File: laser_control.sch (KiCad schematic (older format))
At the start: 20 parts, among them J1 DB9, P1 CONN_01X05, Q1 BC846A, Q2 BC846A, U1 74HCT02, U2 H11L1, U3 H11L1

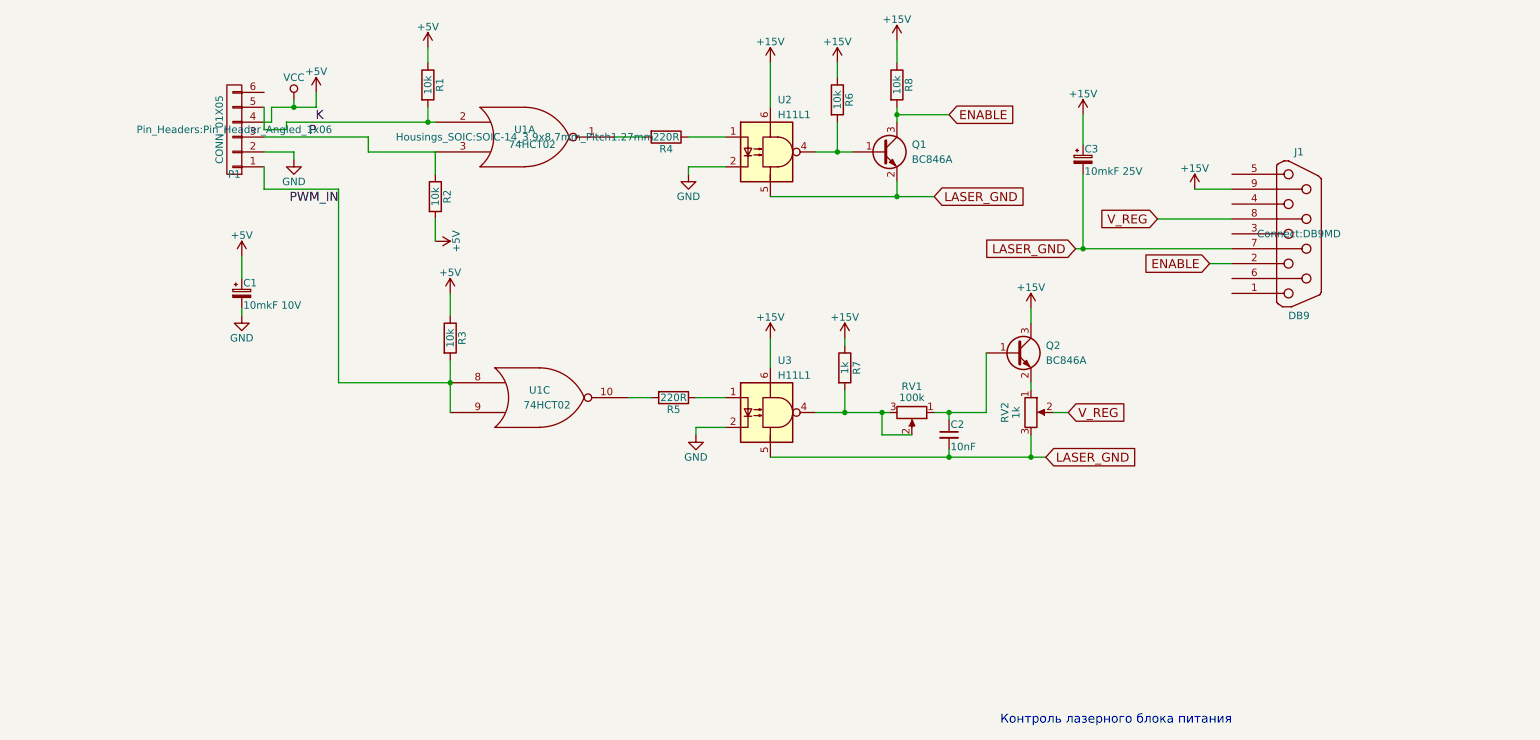
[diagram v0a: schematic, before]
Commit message: Minimal viable modifications
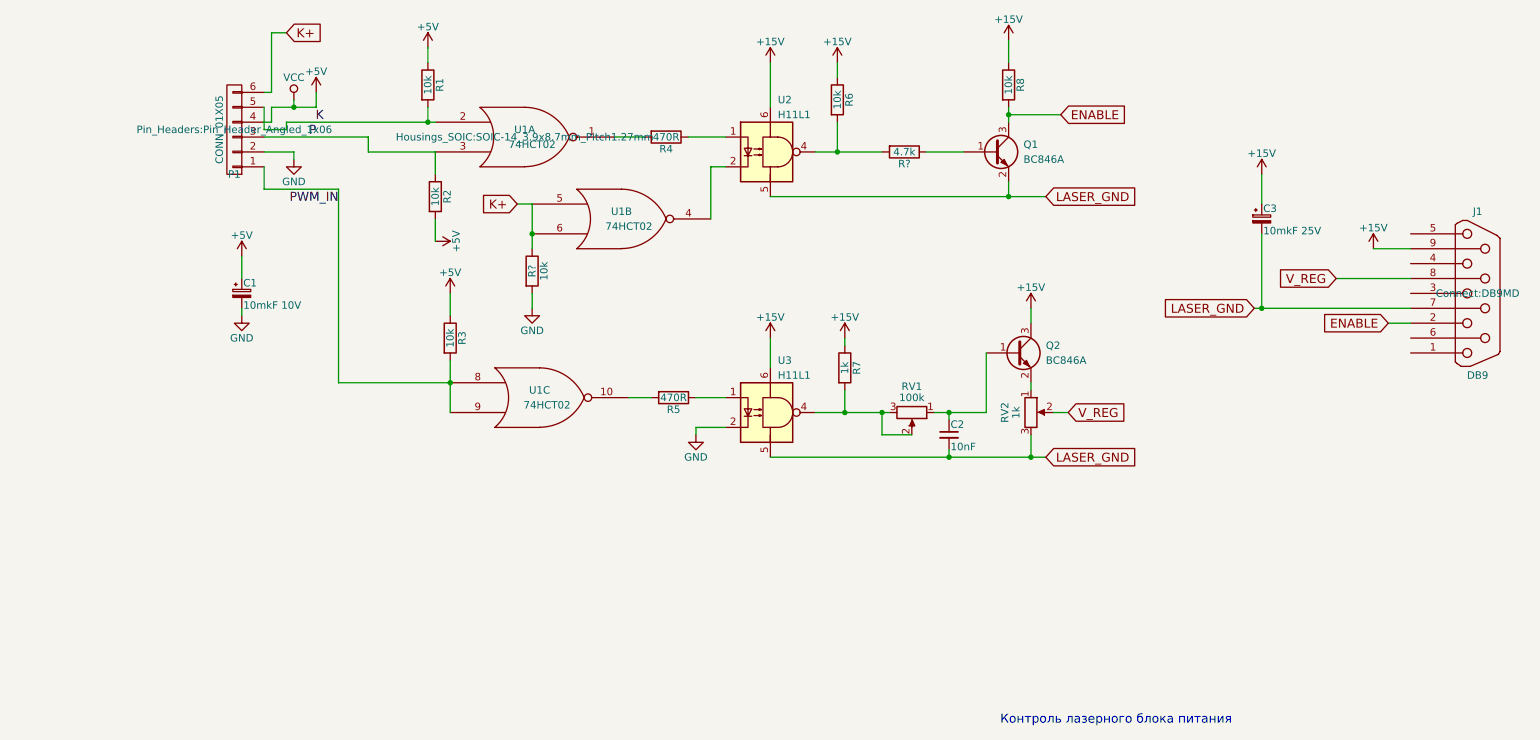
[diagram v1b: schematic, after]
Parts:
- added 10k: R?, Resistors_SMD:R_0805_HandSoldering, symbol R
- added R?: 4.7k, Resistors_SMD:R_0805_HandSoldering, symbol R
- added unit 2 of U1
- R4, R5: value 220R -> 470R
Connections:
- net +5V: now also U1.14 (VCC)
- net GND: now also 10k.2, U1.7 (GND); no longer U2.2
- net at R6.2, U2.4: now also R?.2; no longer Q1.1 (B)
- net K+: now reaches P1.6 (P6)
- net K+: now also 10k.1, U1.5, U1.6
- new net: U1.4, U2.2
- new net: Q1.1 (B), R?.1
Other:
- moved on the sheet: C3, J1, Q1, R8
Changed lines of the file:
@@
 L DB9 J1
 U 1 1 5C063D4D
-P 9500 4200
-F 0 "J1" H 9500 4750 50  0000 C CNN
-F 1 "DB9" H 9500 3650 50  0000 C CNN
-F 2 "Connect:DB9MD" H 9500 4200 50  0000 C CNN
-F 3 "" H 9500 4200 50  0000 C CNN
-	1    9500 4200
+P 10700 4600
+F 0 "J1" H 10700 5150 50  0000 C CNN
+F 1 "DB9" H 10700 4050 50  0000 C CNN
+F 2 "Connect:DB9MD" H 10700 4600 50  0000 C CNN
+F 3 "" H 10700 4600 50  0000 C CNN
+	1    10700 4600
 	1    0    0    -1
 $EndComp
@@
 L Q_NPN_BEC Q1
 U 1 1 5C063F42
-P 6700 3650
-F 0 "Q1" H 6900 3700 50  0000 L CNN
-F 1 "BC846A" H 6900 3600 50  0000 L CNN
-F 2 "TO_SOT_Packages_SMD:SOT-23" H 6900 3750 50  0001 C CNN
-F 3 "" H 6700 3650 50  0001 C CNN
-	1    6700 3650
+P 7450 3650
+F 0 "Q1" H 7650 3700 50  0000 L CNN
+F 1 "BC846A" H 7650 3600 50  0000 L CNN
+F 2 "TO_SOT_Packages_SMD:SOT-23" H 7650 3750 50  0001 C CNN
+F 3 "" H 7450 3650 50  0001 C CNN
+	1    7450 3650
 	1    0    0    -1
 $EndComp
@@
 L +15V #PWR01
 U 1 1 5C064296
-P 8800 3900
-F 0 "#PWR01" H 8800 3750 50  0001 C CNN
-F 1 "+15V" H 8800 4040 50  0000 C CNN
-F 2 "" H 8800 3900 50  0001 C CNN
-F 3 "" H 8800 3900 50  0001 C CNN
-	1    8800 3900
+P 10000 4300
+F 0 "#PWR01" H 10000 4150 50  0001 C CNN
+F 1 "+15V" H 10000 4440 50  0000 C CNN
+F 2 "" H 10000 4300 50  0001 C CNN
+F 3 "" H 10000 4300 50  0001 C CNN
+	1    10000 4300
 	1    0    0    -1
 $EndComp
@@
 L R R8
 U 1 1 5C064446
-P 6800 3200
-F 0 "R8" V 6880 3200 50  0000 C CNN
-F 1 "10k" V 6800 3200 50  0000 C CNN
-F 2 "Resistors_ThroughHole:Resistor_Horizontal_RM10mm" V 6730 3200 50  0001 C CNN
-F 3 "" H 6800 3200 50  0001 C CNN
-	1    6800 3200
+P 7550 3200
+F 0 "R8" V 7630 3200 50  0000 C CNN
+F 1 "10k" V 7550 3200 50  0000 C CNN
+F 2 "Resistors_ThroughHole:Resistor_Horizontal_RM10mm" V 7480 3200 50  0001 C CNN
+F 3 "" H 7550 3200 50  0001 C CNN
+	1    7550 3200
 	1    0    0    -1
 $EndComp
@@
 L +15V #PWR05
 U 1 1 5C06450F
-P 6800 2900
-F 0 "#PWR05" H 6800 2750 50  0001 C CNN
-F 1 "+15V" H 6800 3040 50  0000 C CNN
-F 2 "" H 6800 2900 50  0001 C CNN
-F 3 "" H 6800 2900 50  0001 C CNN
-	1    6800 2900
-	1    0    0    -1
-$EndComp
-Text GLabel 7050 3950 2    60   Input ~ 0
+P 7550 2900
+F 0 "#PWR05" H 7550 2750 50  0001 C CNN
+F 1 "+15V" H 7550 3040 50  0000 C CNN
+F 2 "" H 7550 2900 50  0001 C CNN
+F 3 "" H 7550 2900 50  0001 C CNN
+	1    7550 2900
+	1    0    0    -1
+$EndComp
+Text GLabel 7800 3950 2    60   Input ~ 0
 LASER_GND
-Text GLabel 8000 4300 0    60   Input ~ 0
+Text GLabel 9200 4700 0    60   Input ~ 0
 LASER_GND
-Text GLabel 7150 3400 2    60   Input ~ 0
+Text GLabel 7900 3400 2    60   Input ~ 0
 ENABLE
-Text GLabel 8900 4400 0    60   Input ~ 0
+Text GLabel 10100 4800 0    60   Input ~ 0
 ENABLE
-Text GLabel 8550 4100 0    60   Input ~ 0
+Text GLabel 9750 4500 0    60   Input ~ 0
 V_REG
 $Comp
@@
 P 5250 3550
 F 0 "R4" V 5330 3550 50  0000 C CNN
-F 1 "220R" V 5250 3550 50  0000 C CNN
+F 1 "470R" V 5250 3550 50  0000 C CNN
 F 2 "Resistors_SMD:R_0805_HandSoldering" V 5180 3550 50  0001 C CNN
 F 3 "" H 5250 3550 50  0001 C CNN
@@
 LASER_GND
 Wire Wire Line
-	6250 3650 6500 3650
+	6250 3650 6700 3650
 Connection ~ 6400 3650
 Wire Wire Line
-	8000 4300 9050 4300
-Wire Wire Line
-	6800 3850 6800 3950
-Wire Wire Line
-	8800 3900 9050 3900
+	9200 4700 10250 4700
+Wire Wire Line
+	7550 3850 7550 3950
+Wire Wire Line
+	10000 4300 10250 4300
 Wire Wire Line
 	6400 3050 6400 3150
@@
 	5950 4900 5950 5100
 Wire Wire Line
-	6800 3350 6800 3450
-Wire Wire Line
-	6800 2900 6800 3050
-Wire Wire Line
-	5950 3950 7050 3950
-Connection ~ 6800 3950
-Wire Wire Line
-	6400 3450 6400 3650
-Wire Wire Line
-	6800 3400 7150 3400
-Connection ~ 6800 3400
-Wire Wire Line
-	8900 4400 9050 4400
-Wire Wire Line
-	8550 4100 9050 4100
+	7550 3350 7550 3450
+Wire Wire Line
+	7550 2900 7550 3050
+Wire Wire Line
+	5950 3950 7800 3950
+Connection ~ 7550 3950
+Wire Wire Line
+	6400 3650 6400 3450
+Wire Wire Line
+	7550 3400 7900 3400
+Connection ~ 7550 3400
+Wire Wire Line
+	10100 4800 10250 4800
+Wire Wire Line
+	9750 4500 10250 4500
 Wire Wire Line
 	5400 3550 5650 3550
@@
 P 5300 5300
 F 0 "R5" V 5380 5300 50  0000 C CNN
-F 1 "220R" V 5300 5300 50  0000 C CNN
+F 1 "470R" V 5300 5300 50  0000 C CNN
 F 2 "Resistors_SMD:R_0805_HandSoldering" V 5230 5300 50  0001 C CNN
 F 3 "" H 5300 5300 50  0001 C CNN
@@
 	3800 5050 3800 5400
 Wire Wire Line
-	5400 3750 5650 3750
-Wire Wire Line
-	5400 3750 5400 3800
-Wire Wire Line
 	5650 5500 5450 5500
 Wire Wire Line
 	5450 5500 5450 5550
-$Comp
-L GND #PWR07
-U 1 1 5C0659F6
-P 5400 3800
-F 0 "#PWR07" H 5400 3550 50  0001 C CNN
-F 1 "GND" H 5400 3650 50  0000 C CNN
-F 2 "" H 5400 3800 50  0001 C CNN
-F 3 "" H 5400 3800 50  0001 C CNN
-	1    5400 3800
-	1    0    0    -1
-$EndComp
 $Comp
 L GND #PWR08
@@
 L CP_Small C3
 U 1 1 5C0675C7
-P 8050 3700
-F 0 "C3" H 8060 3770 50  0000 L CNN
-F 1 "10mkF 25V" H 8060 3620 50  0000 L CNN
-F 2 "Capacitors_SMD:c_elec_6.3x5.3" H 8050 3700 50  0001 C CNN
-F 3 "" H 8050 3700 50  0001 C CNN
-	1    8050 3700
+P 9250 4100
+F 0 "C3" H 9260 4170 50  0000 L CNN
+F 1 "10mkF 25V" H 9260 4020 50  0000 L CNN
+F 2 "Capacitors_SMD:c_elec_6.3x5.3" H 9250 4100 50  0001 C CNN
+F 3 "" H 9250 4100 50  0001 C CNN
+	1    9250 4100
 	1    0    0    -1
 $EndComp
@@
 L +15V #PWR017
 U 1 1 5C067662
-P 8050 3400
-F 0 "#PWR017" H 8050 3250 50  0001 C CNN
-F 1 "+15V" H 8050 3540 50  0000 C CNN
-F 2 "" H 8050 3400 50  0001 C CNN
-F 3 "" H 8050 3400 50  0001 C CNN
-	1    8050 3400
-	1    0    0    -1
-$EndComp
-Wire Wire Line
-	8050 3800 8050 4300
-Connection ~ 8050 4300
-Wire Wire Line
-	8050 3400 8050 3600
+P 9250 3800
+F 0 "#PWR017" H 9250 3650 50  0001 C CNN
+F 1 "+15V" H 9250 3940 50  0000 C CNN
+F 2 "" H 9250 3800 50  0001 C CNN
+F 3 "" H 9250 3800 50  0001 C CNN
+	1    9250 3800
+	1    0    0    -1
+$EndComp
+Wire Wire Line
+	9250 4200 9250 4700
+Connection ~ 9250 4700
+Wire Wire Line
+	9250 3800 9250 4000
 Text Notes 9050 7500 2    60   ~ 0
 Контроль лазерного блока питания
@@
 Wire Wire Line
 	2750 3650 2550 3650
+$Comp
+L 74HCT02 U1
+U 2 1 5C276FC0
+P 4950 4100
+F 0 "U1" H 4950 4150 50  0000 C CNN
+F 1 "74HCT02" H 5000 4050 50  0000 C CNN
+F 2 "" H 4950 4100 50  0000 C CNN
+F 3 "" H 4950 4100 50  0000 C CNN
+	2    4950 4100
+	1    0    0    -1
+$EndComp
+Wire Wire Line
+	4350 4000 4350 4300
+$Comp
+L R 10k
+U 1 1 5C277267
+P 4350 4450
+F 0 "10k" V 4430 4450 50  0000 C CNN
+F 1 "R?" V 4350 4450 50  0000 C CNN
+F 2 "Resistors_SMD:R_0805_HandSoldering" V 4280 4450 50  0001 C CNN
+F 3 "" H 4350 4450 50  0001 C CNN
+	1    4350 4450
+	1    0    0    -1
+$EndComp
+Connection ~ 4350 4200
+Wire Wire Line
+	4350 4600 4350 4700
+$Comp
+L GND #PWR?
+U 1 1 5C2773F5
+P 4350 4700
+F 0 "#PWR?" H 4350 4450 50  0001 C CNN
+F 1 "GND" H 4350 4550 50  0000 C CNN
+F 2 "" H 4350 4700 50  0001 C CNN
+F 3 "" H 4350 4700 50  0001 C CNN
+	1    4350 4700
+	1    0    0    -1
+$EndComp
+Wire Wire Line
+	2550 3250 2600 3250
+Wire Wire Line
+	2600 3250 2600 2850
+Wire Wire Line
+	2600 2850 2700 2850
+Text GLabel 2700 2850 2    60   Input ~ 0
+K+
+Wire Wire Line
+	5650 3750 5550 3750
+Wire Wire Line
+	5550 3750 5550 4100
+Wire Wire Line
+	4350 4000 4250 4000
+Text GLabel 4250 4000 0    60   Input ~ 0
+K+
+$Comp
+L R R?
+U 1 1 5C277CF8
+P 6850 3650
+F 0 "R?" V 6930 3650 50  0000 C CNN
+F 1 "4.7k" V 6850 3650 50  0000 C CNN
+F 2 "Resistors_SMD:R_0805_HandSoldering" V 6780 3650 50  0001 C CNN
+F 3 "" H 6850 3650 50  0001 C CNN
+	1    6850 3650
+	0    1    1    0
+$EndComp
+Wire Wire Line
+	7000 3650 7250 3650
 $EndSCHEMATC

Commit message: Control with feedback
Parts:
- removed Q2: BC846A, TO_SOT_Packages_SMD:SOT-23, symbol Q_NPN_BEC
- added C4: 0.47uF, Capacitors_SMD:C_0805_HandSoldering, symbol C
- added R10: 100k, Resistors_ThroughHole:Resistor_Horizontal_RM10mm, symbol R
- added S1: button1, local:button1, symbol button1
- added U4: LM358, Housings_SOIC:SOIC-8_3.9x4.9mm_Pitch1.27mm, symbol LM358
- R11: renamed from 10k; value R? -> 10k; footprint Resistors_SMD:R_0805_HandSoldering -> Resistors_ThroughHole:Resistor_Horizontal_RM10mm
- R7: footprint Resistors_ThroughHole:Resistor_Horizontal_RM10mm -> Resistors_SMD:R_0805_HandSoldering
- gave numbers to parts that had none: 1
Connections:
- net +15V: now also U4.8 (V+), U4.8 (V+)
- net +5V: now also S1.5; no longer R3.1
- net GND: now also R3.1, S1.2
- net K: now also U1.5, S1.3; no longer U1.2
- net K+: now also U1.2, U1.3, S1.4; no longer U1.5, U1.6
- net LASER_GND: now also U4.4 (V-), U4.4 (V-)
- net P: now also U1.6; no longer U1.3
- net V_REG: now also C4.1, U4.1; no longer RV2.2
- net at U2.2: now also U1.1; no longer U1.4
- net at R4.2: now also U1.4; no longer U1.1
- net V_FB: now reaches J1.6 (P6)
- net V_FB: now also R10.1
- net at C2.1, RV1.1: now also U4.5 (+)
- net at RV2.1: now also U4.6 (-), U4.7
- new net: RV2.2, U4.3 (+)
- new net: C4.2, R10.2, U4.2 (-)
- no-connect marks 0 -> 2
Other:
- moved on the sheet: RV2

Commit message: Kicad 5 updates
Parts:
- C1, C3: symbol CP_Small -> device:CP_Small
- C2: symbol C_Small -> device:C_Small
- C4: symbol C -> device:C
- J1: symbol DB9 -> laser_control-rescue:DB9
- P1: symbol CONN_01X06 -> laser_control-rescue:CONN_01X06
- Q1: symbol Q_NPN_BEC -> device:Q_NPN_BEC
- R1, R10, R11, R2, R3, R4, R5, R6, R7, R8, R9: symbol R -> device:R
- RV1, RV2: symbol POT -> device:POT
- S1: symbol button1 -> laser_control-rescue:button1
- U1: symbol 74HCT02 -> laser_control-rescue:74HCT02
- U2, U3: symbol H11L1 -> opto:H11L1
- U4: symbol LM358 -> linear:LM358
